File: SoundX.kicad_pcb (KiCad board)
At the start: 2 copper layers, 60.8 x 99.9 mm, 51 parts, among them CN1 EDGE_CONN, CN2 AUDIO_OUT, CN3 CONN_MIDI_IN, CN4 CONN_MIDI_OUT, U1 GAL20V8, U2 MC6850, U3 YM3526, U4 6N138, U6 YM3014, U7 LM324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

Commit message: Final touches for V2
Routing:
- net /phi2: track 36.5 -> 39.3 mm
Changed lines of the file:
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@@
 		(tags "Inductor Radial series Radial pin pitch 4.00mm  diameter 6.0mm")
 		(property "Reference" "FB3"
-			(at 2 4.191 360)
+			(at 2 4.191 0)
 			(layer "F.SilkS")
 			(effects
@@
 		)
 		(property "Value" "FERRITE"
-			(at 2 4.25 360)
+			(at 2 4.25 0)
 			(layer "F.Fab")
 			(effects
@@
 		)
 		(fp_text user "${REFERENCE}"
-			(at 2 0 360)
+			(at 2 0 0)
 			(layer "F.Fab")
 			(effects
@@
 	)
 	(segment
-		(start 149.479 112.395)
-		(end 149.479 98.425)
+		(start 166.177 144.018)
+		(end 166.177 137.861)
 		(width 0.25)
 		(layer "F.Cu")
@@
 	)
 	(segment
-		(start 171.577 120.521604)
-		(end 170.434 119.378604)
+		(start 149.479 112.395)
+		(end 149.479 98.425)
 		(width 0.25)
 		(layer "F.Cu")
@@
 	)
 	(segment
-		(start 170.434 119.378604)
-		(end 170.434 110.363)
+		(start 171.577 132.461)
+		(end 171.577 118.237)
 		(width 0.25)
 		(layer "F.Cu")
@@
 	)
 	(segment
-		(start 171.577 132.461)
-		(end 171.577 120.521604)
+		(start 171.577 118.237)
+		(end 170.434 117.094)
 		(width 0.25)
 		(layer "F.Cu")
@@
 	)
 	(segment
-		(start 166.177 144.018)
-		(end 166.177 137.861)
+		(start 170.434 117.094)
+		(end 170.434 110.363)
 		(width 0.25)
 		(layer "F.Cu")
@@
 	)
 	(segment
-		(start 166.177 137.861)
-		(end 171.577 132.461)
+		(start 172.974 98.425)
+		(end 172.974 94.615)
 		(width 0.25)
 		(layer "F.Cu")
@@
 	)
 	(segment
-		(start 172.974 98.425)
-		(end 172.974 94.615)
+		(start 170.434 110.363)
+		(end 172.974 107.823)
 		(width 0.25)
 		(layer "F.Cu")
@@
 	)
 	(segment
-		(start 170.434 110.363)
-		(end 172.974 107.823)
+		(start 166.177 137.861)
+		(end 171.577 132.461)
 		(width 0.25)
 		(layer "F.Cu")
@@
 	)
 	(segment
-		(start 174.117 132.461)
-		(end 168.177 138.401)
+		(start 173.609 108.204)
+		(end 171.069 110.744)
 		(width 0.25)
 		(layer "F.Cu")
@@
 	)
 	(segment
-		(start 171.069 110.744)
-		(end 171.069 117.475)
+		(start 174.117 119.761)
+		(end 174.117 132.461)
 		(width 0.25)
 		(layer "F.Cu")
@@
 	)
 	(segment
-		(start 171.069 117.475)
-		(end 174.117 120.523)
+		(start 173.609 93.853)
+		(end 173.609 108.204)
 		(width 0.25)
 		(layer "F.Cu")
@@
 	)
 	(segment
-		(start 148.844 95.885)
-		(end 148.844 109.855)
+		(start 174.117 132.461)
+		(end 168.177 138.401)
 		(width 0.25)
 		(layer "F.Cu")
@@
 	)
 	(segment
-		(start 173.609 108.204)
-		(end 171.069 110.744)
+		(start 171.069 110.744)
+		(end 171.069 116.713)
 		(width 0.25)
 		(layer "F.Cu")
@@
 	)
 	(segment
-		(start 174.117 120.523)
-		(end 174.117 132.461)
+		(start 148.844 95.885)
+		(end 148.844 109.855)
 		(width 0.25)
 		(layer "F.Cu")
@@
 	)
 	(segment
-		(start 173.609 93.853)
-		(end 173.609 108.204)
+		(start 171.069 116.713)
+		(end 174.117 119.761)
 		(width 0.25)
 		(layer "F.Cu")
@@
 	)
 	(segment
-		(start 177.165 117.856)
-		(end 180.467 121.158)
+		(start 175.387 112.395)
+		(end 173.609 114.173)
 		(width 0.25)
 		(layer "F.Cu")
@@
 	)
 	(segment
-		(start 175.387 112.395)
-		(end 177.165 114.173)
+		(start 173.609 115.189)
+		(end 180.467 122.047)
 		(width 0.25)
 		(layer "F.Cu")
@@
 	)
 	(segment
-		(start 180.467 121.158)
-		(end 180.467 122.555)
+		(start 174.177 138.878)
+		(end 174.244 138.811)
 		(width 0.25)
 		(layer "F.Cu")
@@
 	)
 	(segment
-		(start 177.165 114.173)
-		(end 177.165 117.856)
+		(start 174.177 144.018)
+		(end 174.177 138.878)
 		(width 0.25)
 		(layer "F.Cu")
@@
 	)
 	(segment
-		(start 174.177 138.878)
-		(end 174.244 138.811)
+		(start 173.609 114.173)
+		(end 173.609 115.189)
 		(width 0.25)
 		(layer "F.Cu")
@@
 	)
 	(segment
-		(start 174.177 144.018)
-		(end 174.177 138.878)
+		(start 180.467 122.047)
+		(end 180.467 123.825)
 		(width 0.25)
 		(layer "F.Cu")
@@
 	)
 	(segment
-		(start 172.339 116.586)
-		(end 172.339 112.395)
-		(width 0.25)
-		(layer "F.Cu")
-		(net 27)
-	)
-	(segment
-		(start 172.339 116.586)
-		(end 176.657 120.904)
-		(width 0.25)
-		(layer "F.Cu")
-		(net 27)
-	)
-	(segment
-		(start 176.657 121.158)
-		(end 176.657 128.778)
+		(start 176.657 120.269)
+		(end 176.657 130.175)
 		(width 0.25)
 		(layer "F.Cu")
@@
 	)
 	(segment
-		(start 176.657 128.778)
-		(end 176.657 130.175)
+		(start 176.657 130.175)
+		(end 177.927 131.445)
 		(width 0.25)
 		(layer "F.Cu")
@@
 	)
 	(segment
-		(start 176.657 120.904)
-		(end 176.657 121.158)
+		(start 172.339 115.951)
+		(end 176.657 120.269)
 		(width 0.25)
 		(layer "F.Cu")
@@
 	)
 	(segment
-		(start 176.657 130.175)
-		(end 177.927 131.445)
+		(start 172.339 112.395)
+		(end 172.339 115.951)
 		(width 0.25)
 		(layer "F.Cu")
@@
 	)
 	(segment
-		(start 173.736012 115.570012)
-		(end 173.736012 115.57)
-		(width 0.25)
-		(layer "F.Cu")
-		(net 30)
-	)
-	(segment
-		(start 179.197 132.461)
-		(end 179.197 121.031)
+		(start 172.177 139.481)
+		(end 179.197 132.461)
 		(width 0.25)
 		(layer "F.Cu")
@@
 	)
 	(segment
-		(start 179.197 121.031)
-		(end 175.768 117.602)
-		(width 0.25)
-		(layer "F.Cu")
-		(net 30)
-	)
-	(segment
-		(start 175.768 117.602)
-		(end 173.736012 115.570012)
+		(start 172.177 144.018)
+		(end 172.177 139.481)
 		(width 0.25)
 		(layer "F.Cu")
@@
 	)
 	(segment
-		(start 172.177 139.481)
-		(end 179.197 132.461)
+		(start 179.197 121.793)
+		(end 172.974 115.57)
 		(width 0.25)
 		(layer "F.Cu")
@@
 	)
 	(segment
-		(start 172.177 144.018)
-		(end 172.177 139.481)
+		(start 179.197 132.461)
+		(end 179.197 121.793)
 		(width 0.25)
 		(layer "F.Cu")
@@
 	)
 	(via
-		(at 173.736012 115.57)
+		(at 172.974 115.57)
 		(size 0.6)
 		(drill 0.4)
@@
 	)
 	(segment
-		(start 173.736012 115.57)
-		(end 164.592 115.57)
+		(start 127.881 59.182)
+		(end 126.357 57.658)
 		(width 0.25)
 		(layer "B.Cu")
@@
 	)
 	(segment
-		(start 127.881 59.182)
-		(end 126.357 57.658)
+		(start 142.494 59.182)
+		(end 127.881 59.182)
 		(width 0.25)
 		(layer "B.Cu")
@@
 	)
 	(segment
-		(start 142.494 59.182)
-		(end 127.881 59.182)
+		(start 164.592 115.57)
+		(end 172.974 115.57)
 		(width 0.25)
 		(layer "B.Cu")
@@
 	)
 	(segment
-		(start 175.387 121.158)
-		(end 175.387 120.523)
-		(width 0.25)
-		(layer "F.Cu")
-		(net 77)
-	)
-	(segment
-		(start 171.704 114.3)
-		(end 171.704 116.84)
+		(start 175.387 120.015)
+		(end 171.704 116.332)
 		(width 0.25)
 		(layer "F.Cu")
@@
 	)
 	(segment
-		(start 175.387 120.523)
-		(end 171.704 116.84)
+		(start 161.925 109.093)
+		(end 161.925 114.299992)
 		(width 0.25)
 		(layer "F.Cu")
@@
 	)
 	(segment
-		(start 161.925 109.093)
-		(end 161.925 114.299992)
+		(start 175.387 122.555)
+		(end 175.387 120.015)
 		(width 0.25)
 		(layer "F.Cu")
@@
 	)
 	(segment
-		(start 175.387 122.555)
-		(end 175.387 121.158)
+		(start 171.704 116.332)
+		(end 171.704 114.3)
 		(width 0.25)
 		(layer "F.Cu")

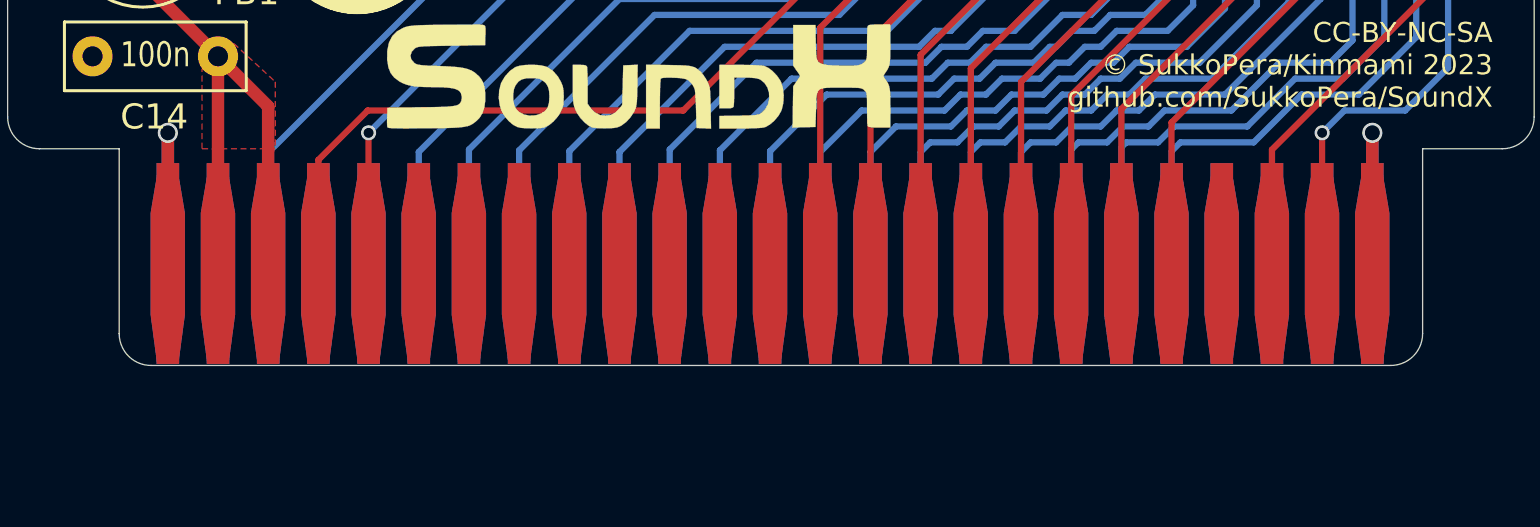
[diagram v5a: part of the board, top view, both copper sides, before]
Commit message: Update edge connector
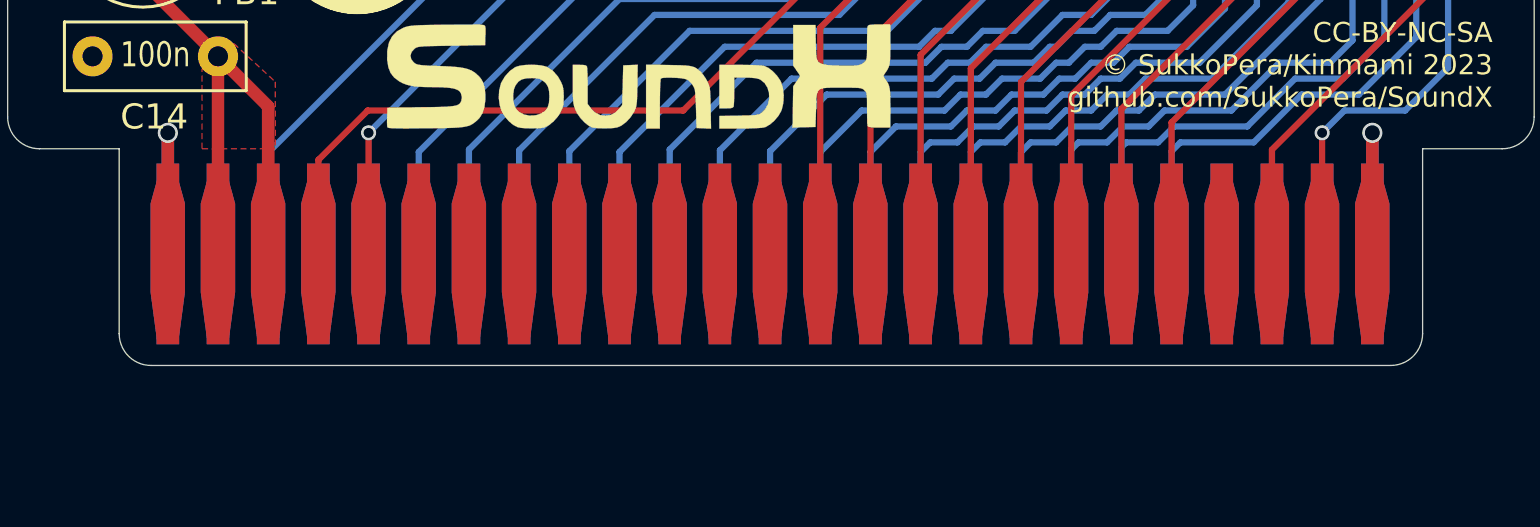
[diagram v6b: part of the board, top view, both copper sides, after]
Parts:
- moved CN1 0.38 mm to (152.2, 143.6)

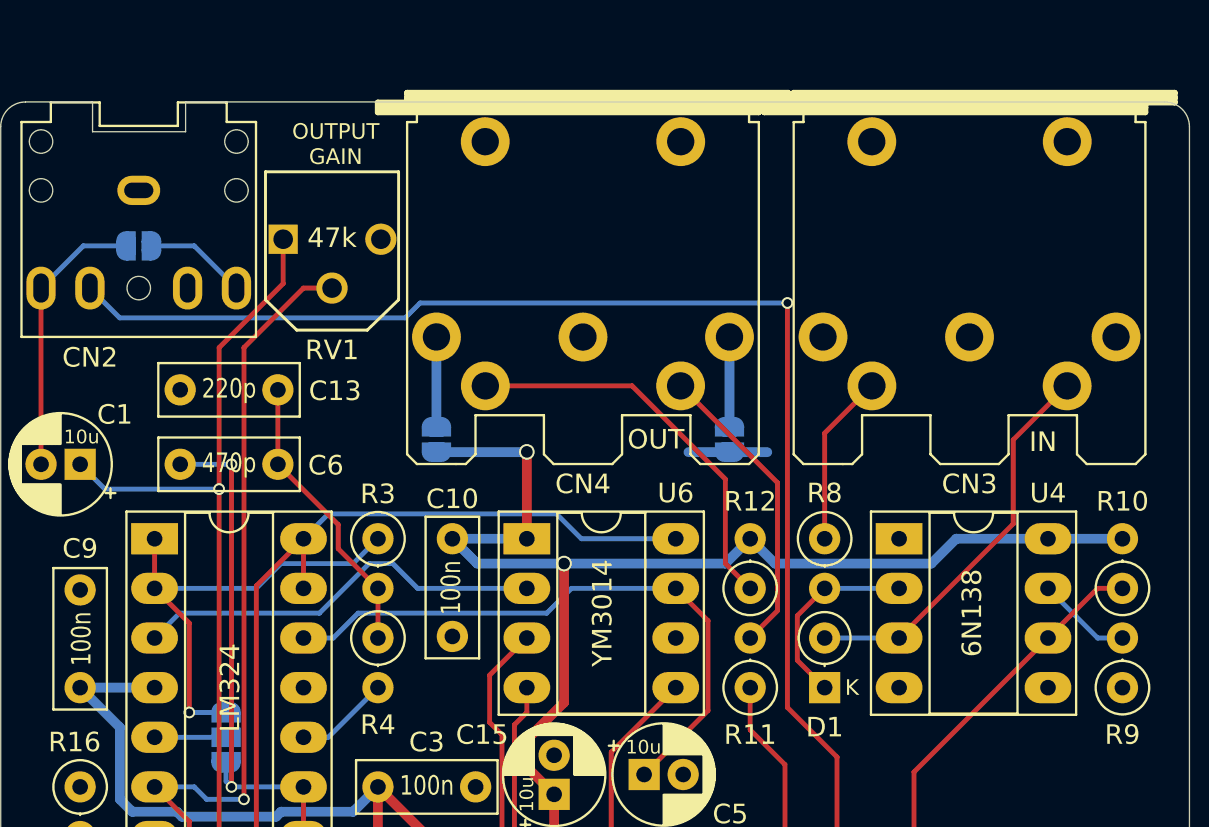
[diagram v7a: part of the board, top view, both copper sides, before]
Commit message: Readd some P/Ns and add 5mm-pitch footprint for DIN-5 connector
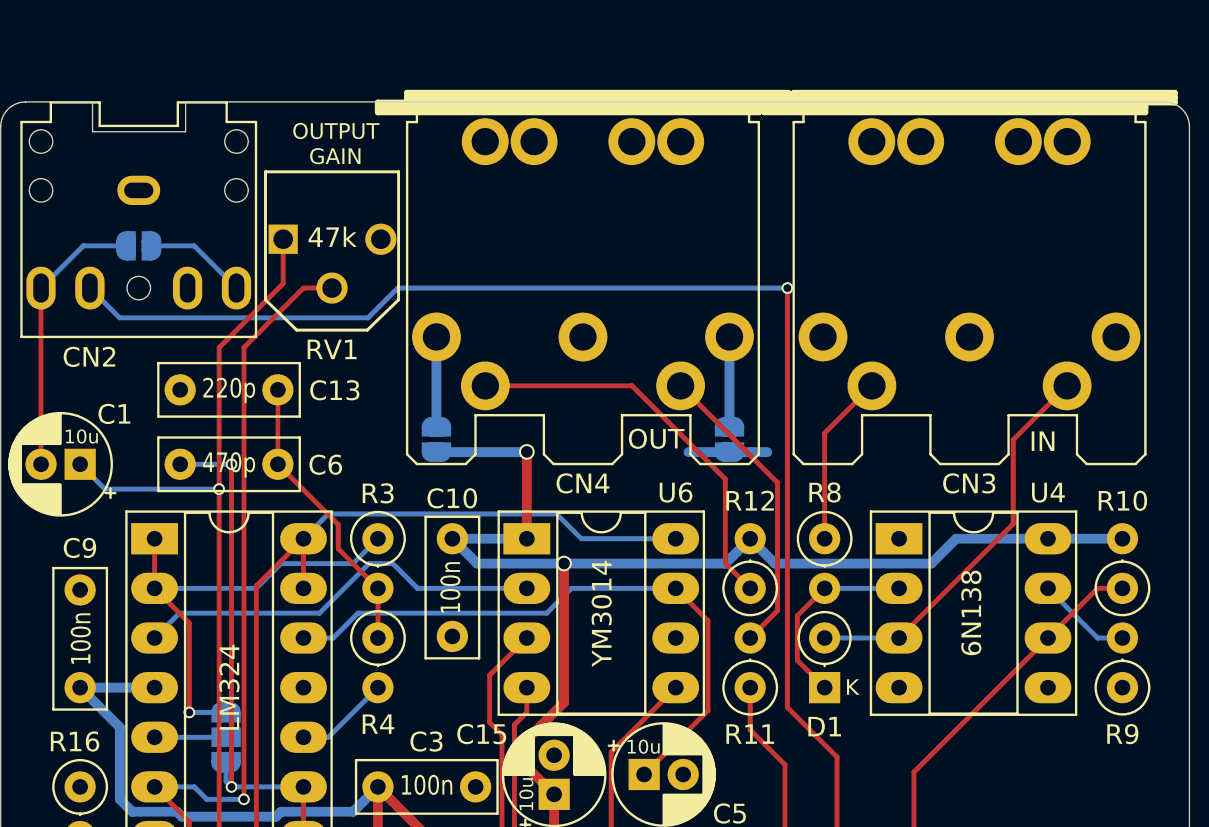
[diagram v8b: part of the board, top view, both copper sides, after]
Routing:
- net /ext_audio: track 137.2 -> 138.2 mm
